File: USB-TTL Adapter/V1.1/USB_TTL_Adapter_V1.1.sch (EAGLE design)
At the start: 3 parts

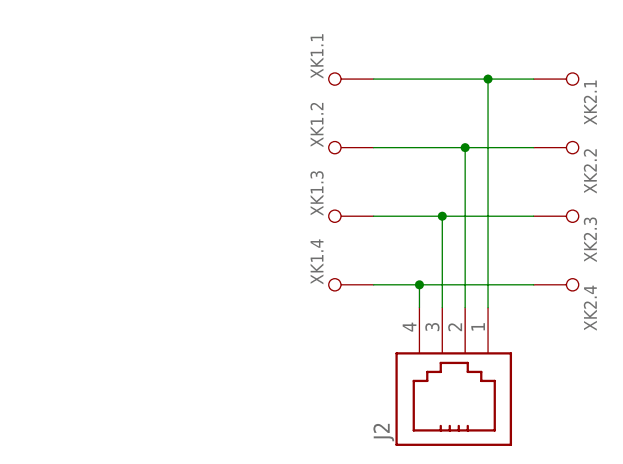
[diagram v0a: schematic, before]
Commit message: 
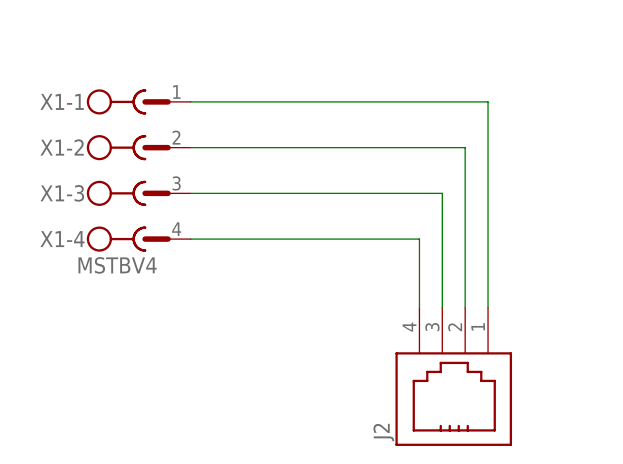
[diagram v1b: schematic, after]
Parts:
- removed XK1, XK2: FKK_4/5.08_LSFSMT5.08/04/1803.5SNBKTU, Federkraftklemme - LSF-SMT5.08:FKK_4/5.08_LSFSMT5.08/04/1803.5SNBKTU
- added X1: MSTBV4, con-phoenix-508:MSTBV4
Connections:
- net N$1: now also X1-4.1; no longer XK1.4..1, XK2.4..1
- net N$2: now also X1-3.1; no longer XK1.3..1, XK2.3..1
- net N$3: now also X1-2.1; no longer XK1.2..1, XK2.2..1
- net N$4: now also X1-1.1; no longer XK1.1..1, XK2.1..1
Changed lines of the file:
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@@
 <parts>
 <part name="J2" library="InputOutputIO (rev18b)" deviceset="615004144021" device=""/>
-<part name="XK1" library="Federkraftklemme - LSF-SMT5.08" deviceset="FKK_4/5.08_LSF" device="SMT5.08/04/1803.5SNBKTU"/>
-<part name="XK2" library="Federkraftklemme - LSF-SMT5.08" deviceset="FKK_4/5.08_LSF" device="SMT5.08/04/1803.5SNBKTU"/>
+<part name="X1" library="con-phoenix-508" deviceset="MSTBV4" device=""/>
 </parts>
 <sheets>
@@
 <instances>
 <instance part="J2" gate="G$1" x="45.72" y="43.18" rot="R90"/>
-<instance part="XK1" gate=".1" x="35.56" y="78.74" rot="R90"/>
-<instance part="XK1" gate=".2" x="35.56" y="71.12" rot="R90"/>
-<instance part="XK1" gate=".3" x="35.56" y="63.5" rot="R90"/>
-<instance part="XK1" gate=".4" x="35.56" y="55.88" rot="R90"/>
-<instance part="XK2" gate=".4" x="53.34" y="55.88" rot="R270"/>
-<instance part="XK2" gate=".3" x="53.34" y="63.5" rot="R270"/>
-<instance part="XK2" gate=".2" x="53.34" y="71.12" rot="R270"/>
-<instance part="XK2" gate=".1" x="53.34" y="78.74" rot="R270"/>
+<instance part="X1" gate="-1" x="10.16" y="76.2"/>
+<instance part="X1" gate="-2" x="10.16" y="71.12"/>
+<instance part="X1" gate="-3" x="10.16" y="66.04"/>
+<instance part="X1" gate="-4" x="10.16" y="60.96"/>
 </instances>
 <busses>
@@
 <segment>
 <pinref part="J2" gate="G$1" pin="4"/>
-<pinref part="XK1" gate=".4" pin=".1"/>
-<wire x1="40.64" y1="53.34" x2="40.64" y2="55.88" width="0.1524" layer="91"/>
-<wire x1="40.64" y1="55.88" x2="35.56" y2="55.88" width="0.1524" layer="91"/>
-<pinref part="XK2" gate=".4" pin=".1"/>
-<wire x1="53.34" y1="55.88" x2="40.64" y2="55.88" width="0.1524" layer="91"/>
-<junction x="40.64" y="55.88"/>
+<pinref part="X1" gate="-4" pin="1"/>
+<wire x1="40.64" y1="53.34" x2="40.64" y2="60.96" width="0.1524" layer="91"/>
+<wire x1="40.64" y1="60.96" x2="15.24" y2="60.96" width="0.1524" layer="91"/>
 </segment>
 </net>
 <net name="N$2" class="0">
 <segment>
-<pinref part="XK1" gate=".3" pin=".1"/>
+<pinref part="X1" gate="-3" pin="1"/>
 <pinref part="J2" gate="G$1" pin="3"/>
-<wire x1="35.56" y1="63.5" x2="43.18" y2="63.5" width="0.1524" layer="91"/>
-<wire x1="43.18" y1="63.5" x2="43.18" y2="53.34" width="0.1524" layer="91"/>
-<pinref part="XK2" gate=".3" pin=".1"/>
-<wire x1="53.34" y1="63.5" x2="43.18" y2="63.5" width="0.1524" layer="91"/>
-<junction x="43.18" y="63.5"/>
+<wire x1="15.24" y1="66.04" x2="43.18" y2="66.04" width="0.1524" layer="91"/>
+<wire x1="43.18" y1="66.04" x2="43.18" y2="53.34" width="0.1524" layer="91"/>
 </segment>
 </net>
 <net name="N$3" class="0">
 <segment>
-<pinref part="XK1" gate=".2" pin=".1"/>
+<pinref part="X1" gate="-2" pin="1"/>
 <pinref part="J2" gate="G$1" pin="2"/>
-<wire x1="35.56" y1="71.12" x2="45.72" y2="71.12" width="0.1524" layer="91"/>
+<wire x1="15.24" y1="71.12" x2="45.72" y2="71.12" width="0.1524" layer="91"/>
 <wire x1="45.72" y1="71.12" x2="45.72" y2="53.34" width="0.1524" layer="91"/>
-<pinref part="XK2" gate=".2" pin=".1"/>
-<wire x1="53.34" y1="71.12" x2="45.72" y2="71.12" width="0.1524" layer="91"/>
-<junction x="45.72" y="71.12"/>
 </segment>
 </net>
 <net name="N$4" class="0">
 <segment>
-<pinref part="XK1" gate=".1" pin=".1"/>
+<pinref part="X1" gate="-1" pin="1"/>
 <pinref part="J2" gate="G$1" pin="1"/>
-<wire x1="35.56" y1="78.74" x2="48.26" y2="78.74" width="0.1524" layer="91"/>
-<wire x1="48.26" y1="78.74" x2="48.26" y2="53.34" width="0.1524" layer="91"/>
-<pinref part="XK2" gate=".1" pin=".1"/>
-<wire x1="53.34" y1="78.74" x2="48.26" y2="78.74" width="0.1524" layer="91"/>
-<junction x="48.26" y="78.74"/>
+<wire x1="15.24" y1="76.2" x2="48.26" y2="76.2" width="0.1524" layer="91"/>
+<wire x1="48.26" y1="76.2" x2="48.26" y2="53.34" width="0.1524" layer="91"/>
 </segment>
 </net>

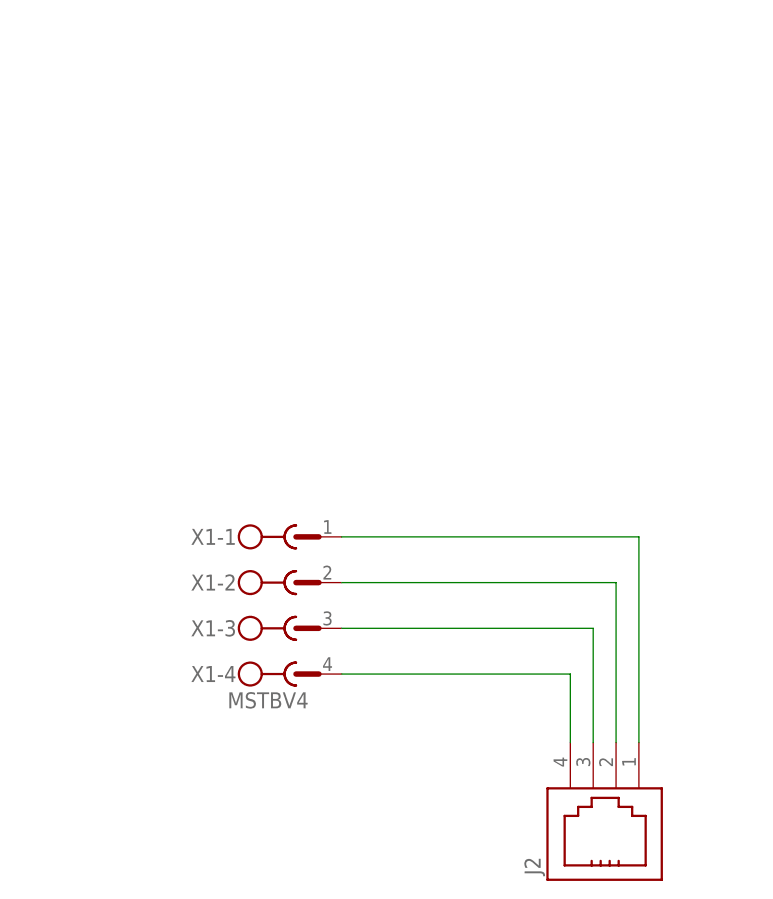
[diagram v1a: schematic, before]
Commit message: 
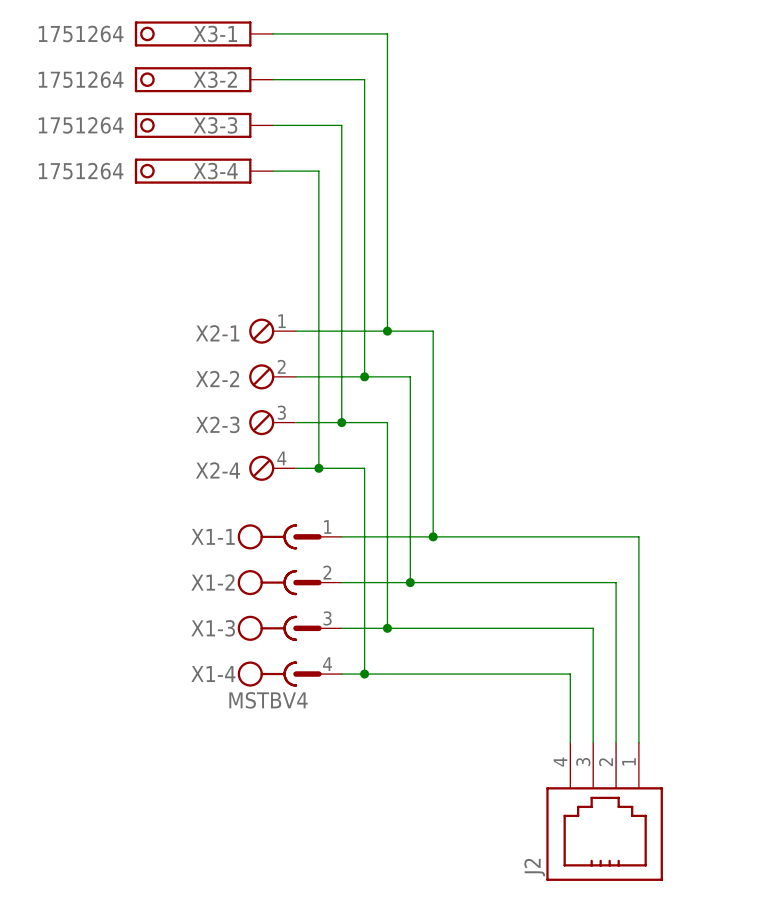
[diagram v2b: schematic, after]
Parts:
- added X2: (no value), con-phoenix-254:MPT4
- added X3: 1751264, con-phoenix-350:1751264
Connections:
- net N$1: now also X2-4.1, X3-4.K
- net N$2: now also X2-3.1, X3-3.K
- net N$3: now also X2-2.1, X3-2.K
- net N$4: now also X2-1.1, X3-1.K
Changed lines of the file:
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@@
 <?xml version="1.0" encoding="utf-8"?>
 <!DOCTYPE eagle SYSTEM "eagle.dtd">
-<eagle version="6.5.0">
+<eagle version="7.7.0">
 <drawing>
 <settings>
@@
 <part name="J2" library="InputOutputIO (rev18b)" deviceset="615004144021" device=""/>
 <part name="X1" library="con-phoenix-508" deviceset="MSTBV4" device=""/>
+<part name="X2" library="con-phoenix-254" deviceset="MPT4" device=""/>
+<part name="X3" library="con-phoenix-350" deviceset="1751264" device=""/>
 </parts>
 <sheets>
@@
 <instance part="X1" gate="-3" x="10.16" y="66.04"/>
 <instance part="X1" gate="-4" x="10.16" y="60.96"/>
+<instance part="X2" gate="-1" x="7.62" y="99.06" rot="R180"/>
+<instance part="X2" gate="-2" x="7.62" y="93.98" rot="R180"/>
+<instance part="X2" gate="-3" x="7.62" y="88.9" rot="R180"/>
+<instance part="X2" gate="-4" x="7.62" y="83.82" rot="R180"/>
+<instance part="X3" gate="-1" x="5.08" y="132.08" rot="R180"/>
+<instance part="X3" gate="-2" x="5.08" y="127" rot="R180"/>
+<instance part="X3" gate="-3" x="5.08" y="121.92" rot="R180"/>
+<instance part="X3" gate="-4" x="5.08" y="116.84" rot="R180"/>
 </instances>
 <busses>
@@
 <pinref part="X1" gate="-4" pin="1"/>
 <wire x1="40.64" y1="53.34" x2="40.64" y2="60.96" width="0.1524" layer="91"/>
-<wire x1="40.64" y1="60.96" x2="15.24" y2="60.96" width="0.1524" layer="91"/>
+<wire x1="40.64" y1="60.96" x2="17.78" y2="60.96" width="0.1524" layer="91"/>
+<pinref part="X2" gate="-4" pin="1"/>
+<wire x1="17.78" y1="60.96" x2="15.24" y2="60.96" width="0.1524" layer="91"/>
+<wire x1="10.16" y1="83.82" x2="12.7" y2="83.82" width="0.1524" layer="91"/>
+<wire x1="12.7" y1="83.82" x2="17.78" y2="83.82" width="0.1524" layer="91"/>
+<wire x1="17.78" y1="83.82" x2="17.78" y2="60.96" width="0.1524" layer="91"/>
+<junction x="17.78" y="60.96"/>
+<pinref part="X3" gate="-4" pin="K"/>
+<wire x1="7.62" y1="116.84" x2="12.7" y2="116.84" width="0.1524" layer="91"/>
+<wire x1="12.7" y1="116.84" x2="12.7" y2="83.82" width="0.1524" layer="91"/>
+<junction x="12.7" y="83.82"/>
 </segment>
 </net>
@@
 <pinref part="X1" gate="-3" pin="1"/>
 <pinref part="J2" gate="G$1" pin="3"/>
-<wire x1="15.24" y1="66.04" x2="43.18" y2="66.04" width="0.1524" layer="91"/>
+<wire x1="15.24" y1="66.04" x2="20.32" y2="66.04" width="0.1524" layer="91"/>
+<wire x1="20.32" y1="66.04" x2="43.18" y2="66.04" width="0.1524" layer="91"/>
 <wire x1="43.18" y1="66.04" x2="43.18" y2="53.34" width="0.1524" layer="91"/>
+<pinref part="X2" gate="-3" pin="1"/>
+<wire x1="10.16" y1="88.9" x2="15.24" y2="88.9" width="0.1524" layer="91"/>
+<wire x1="15.24" y1="88.9" x2="20.32" y2="88.9" width="0.1524" layer="91"/>
+<wire x1="20.32" y1="88.9" x2="20.32" y2="66.04" width="0.1524" layer="91"/>
+<junction x="20.32" y="66.04"/>
+<pinref part="X3" gate="-3" pin="K"/>
+<wire x1="7.62" y1="121.92" x2="15.24" y2="121.92" width="0.1524" layer="91"/>
+<wire x1="15.24" y1="121.92" x2="15.24" y2="88.9" width="0.1524" layer="91"/>
+<junction x="15.24" y="88.9"/>
 </segment>
 </net>
@@
 <pinref part="X1" gate="-2" pin="1"/>
 <pinref part="J2" gate="G$1" pin="2"/>
-<wire x1="15.24" y1="71.12" x2="45.72" y2="71.12" width="0.1524" layer="91"/>
+<wire x1="15.24" y1="71.12" x2="22.86" y2="71.12" width="0.1524" layer="91"/>
+<wire x1="22.86" y1="71.12" x2="45.72" y2="71.12" width="0.1524" layer="91"/>
 <wire x1="45.72" y1="71.12" x2="45.72" y2="53.34" width="0.1524" layer="91"/>
+<pinref part="X2" gate="-2" pin="1"/>
+<wire x1="10.16" y1="93.98" x2="17.78" y2="93.98" width="0.1524" layer="91"/>
+<wire x1="17.78" y1="93.98" x2="22.86" y2="93.98" width="0.1524" layer="91"/>
+<wire x1="22.86" y1="93.98" x2="22.86" y2="71.12" width="0.1524" layer="91"/>
+<junction x="22.86" y="71.12"/>
+<pinref part="X3" gate="-2" pin="K"/>
+<wire x1="7.62" y1="127" x2="17.78" y2="127" width="0.1524" layer="91"/>
+<wire x1="17.78" y1="127" x2="17.78" y2="93.98" width="0.1524" layer="91"/>
+<junction x="17.78" y="93.98"/>
 </segment>
 </net>
@@
 <pinref part="X1" gate="-1" pin="1"/>
 <pinref part="J2" gate="G$1" pin="1"/>
-<wire x1="15.24" y1="76.2" x2="48.26" y2="76.2" width="0.1524" layer="91"/>
+<wire x1="15.24" y1="76.2" x2="25.4" y2="76.2" width="0.1524" layer="91"/>
+<wire x1="25.4" y1="76.2" x2="48.26" y2="76.2" width="0.1524" layer="91"/>
 <wire x1="48.26" y1="76.2" x2="48.26" y2="53.34" width="0.1524" layer="91"/>
+<pinref part="X2" gate="-1" pin="1"/>
+<wire x1="10.16" y1="99.06" x2="20.32" y2="99.06" width="0.1524" layer="91"/>
+<wire x1="20.32" y1="99.06" x2="25.4" y2="99.06" width="0.1524" layer="91"/>
+<wire x1="25.4" y1="99.06" x2="25.4" y2="76.2" width="0.1524" layer="91"/>
+<junction x="25.4" y="76.2"/>
+<pinref part="X3" gate="-1" pin="K"/>
+<wire x1="7.62" y1="132.08" x2="20.32" y2="132.08" width="0.1524" layer="91"/>
+<wire x1="20.32" y1="132.08" x2="20.32" y2="99.06" width="0.1524" layer="91"/>
+<junction x="20.32" y="99.06"/>
 </segment>
 </net>
